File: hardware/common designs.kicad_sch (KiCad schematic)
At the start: 121 parts, among them J401 Conn_01x05_Pin, J402 Main Current Hall Effect Sens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, J403 Conn_02x03_Top_Bottom, K401 G5Q-1A 12Vdc, K402 G5Q-1A 24Vdc, Q401 MMBT5550L, Q402 MMBTA94, Q403 MMBT5550L, Q404 MMBT5550L, Q405 TSM2328CX, Q406 TSM2328CX, Q407 TSM2328CX, Q408 TSM2328CX, U401 IPD70R, U402 NSI45015, U403 MIC7300M5, U404 MCP2542FDxMF, U405 DMN62D0U, U406 IPD14N06, U407 NSI5030, U408 Si1450DH, U409 MCP9700x-ETT, U410 AP7381-33SA-7, U411 ISOM8110DFS, U412 LM74502, U413 TLP176AM, U414 NCV68061, U415 ISO1044BD, U416 TLV713185PDBV, U417 AP64060ZQ, U418 AP64060ZQ, U419 RAA211805, U420 IRS20752, U421 MC7815C, U422 IPD14N06, U423 AP7384-50SA, U501 TC74HC595

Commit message: we love ti
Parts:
- added C501: 1u, Capacitor_SMD:C_0603_1608Metric_Pad1.08x0.95mm_HandSolder, symbol Device:C_Small
- added Q501: DI035P04PT, zzLocalLibraries-Footprints:D_QFN_3.3x3.3mm_P0.65mm, symbol zzLocalLibrary:DI035P04PT
- U411: mouser 1 (none) -> https://www.mouser.com/ProductDetail/Texas-Instruments/ISOM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

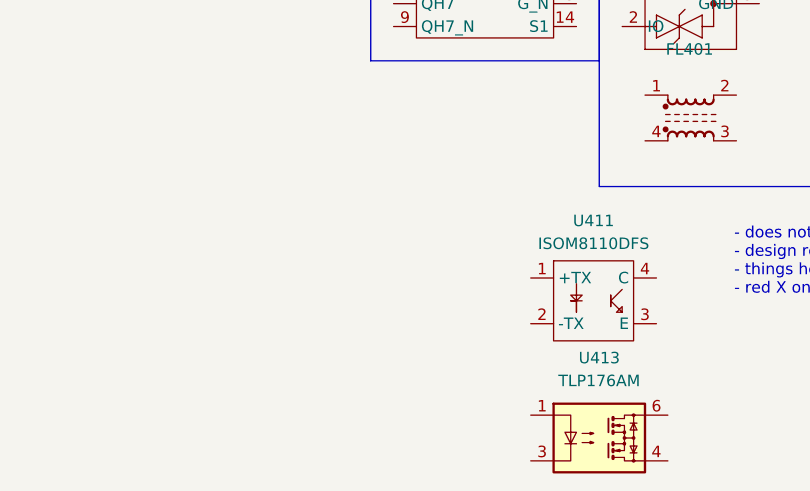
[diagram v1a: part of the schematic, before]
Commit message: new psu
now not under sized
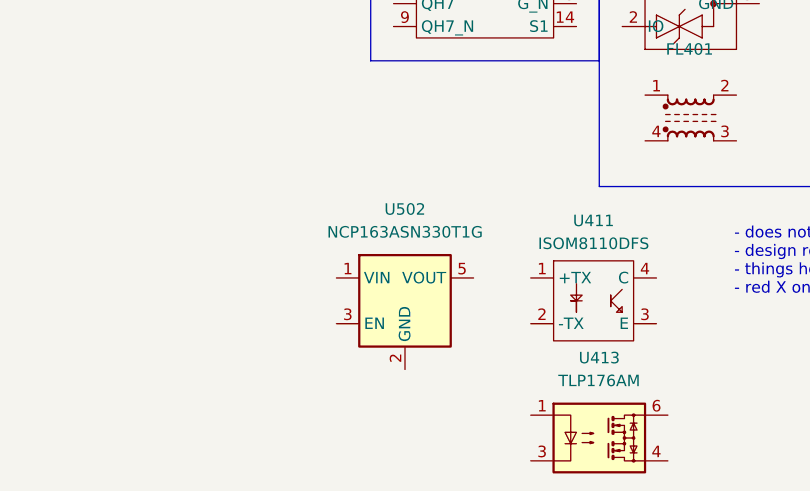
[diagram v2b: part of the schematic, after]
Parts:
- added U502: NCP163ASN330T1G, Package_TO_SOT_SMD:SOT-23-5_HandSoldering, symbol Regulator_Linear:NCP163ASN330T1G

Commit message: lsoing it
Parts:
- removed FL401: Choke_CommonMode_FerriteCore_1243, Inductor_SMD:L_CommonModeChoke_Coilcraft_1812CAN, symbol Filter:Choke_CommonMode_FerriteCore_1243
- added C308: 22u, Capacitor_SMD:C_0805_2012Metric_Pad1.18x1.45mm_HandSolder, symbol Device:C_Small
- added FL801: Choke_CommonMode_FerriteCore_1243, Inductor_SMD:L_CommonModeChoke_Coilcraft_1812CAN, symbol Filter:Choke_CommonMode_FerriteCore_1243
- added R304: 33.2k, Resistor_SMD:R_0805_2012Metric_Pad1.20x1.40mm_HandSolder, symbol Device:R_Small_US
- renumbered C501 to C307, C401 to C801, C402 to C802, C403 to C803, C404 to C804, C405 to C805, C406 to C806, C407 to C807, C408 to C808, C409 to C809, C410 to C810, C411 to C811, C412 to C812, C413 to C813, C414 to C814, C415 to C815, C416 to C816, C417 to C817, C418 to C818, C419 to C819, C420 to C820, C421 to C821, C422 to C822, CR401 to CR801, D401 to D801, D402 to D802, D403 to D803, D404 to D804, D405 to D805, D406 to D806, D407 to D807, D408 to D808, D409 to D809, D410 to D810, D411 to D811, D412 to D812, D413 to D813, D414 to D814, D415 to D815, D416 to D816, FB401 to FB801, FB402 to FB802, J401 to J801, J402 to J802, J403 to J803, K401 to K801, K402 to K802, L401 to L801, L402 to L802, L403 to L803, Q501 to Q303, Q401 to Q801, Q402 to Q802, Q405 to Q803, Q403 to Q804, Q404 to Q805, Q406 to Q806, Q407 to Q807, Q408 to Q808, R401 to R801, R402 to R802, R403 to R803, R404 to R804, R405 to R805, R406 to R806, R407 to R807, R408 to R808, R409 to R809, R410 to R810, R411 to R811, R412 to R812, R413 to R813, R414 to R814, R415 to R815, R416 to R816, R417 to R817, R418 to R818, R419 to R819, R420 to R820, R421 to R821, R422 to R822, R438 to R823, R423 to R824, R424 to R825, R425 to R826, R426 to R827, R427 to R828, R428 to R829, R429 to R830, R430 to R831, R431 to R832, R432 to R833, R433 to R834, R434 to R835, R435 to R836, R436 to R837, R437 to R838, TP401 to TP801, U502 to U302, U501 to U303, U401 to U801, U402 to U802, U403 to U803, U404 to U804, U405 to U805, U406 to U806, U407 to U807, U408 to U808, U409 to U809, U410 to U810, U412 to U811, U414 to U812, U416 to U813, U417 to U814, U418 to U815, U419 to U816, U420 to U817, U421 to U818, U422 to U819, U423 to U820, U415 to U821, U411 to U822, U413 to U823

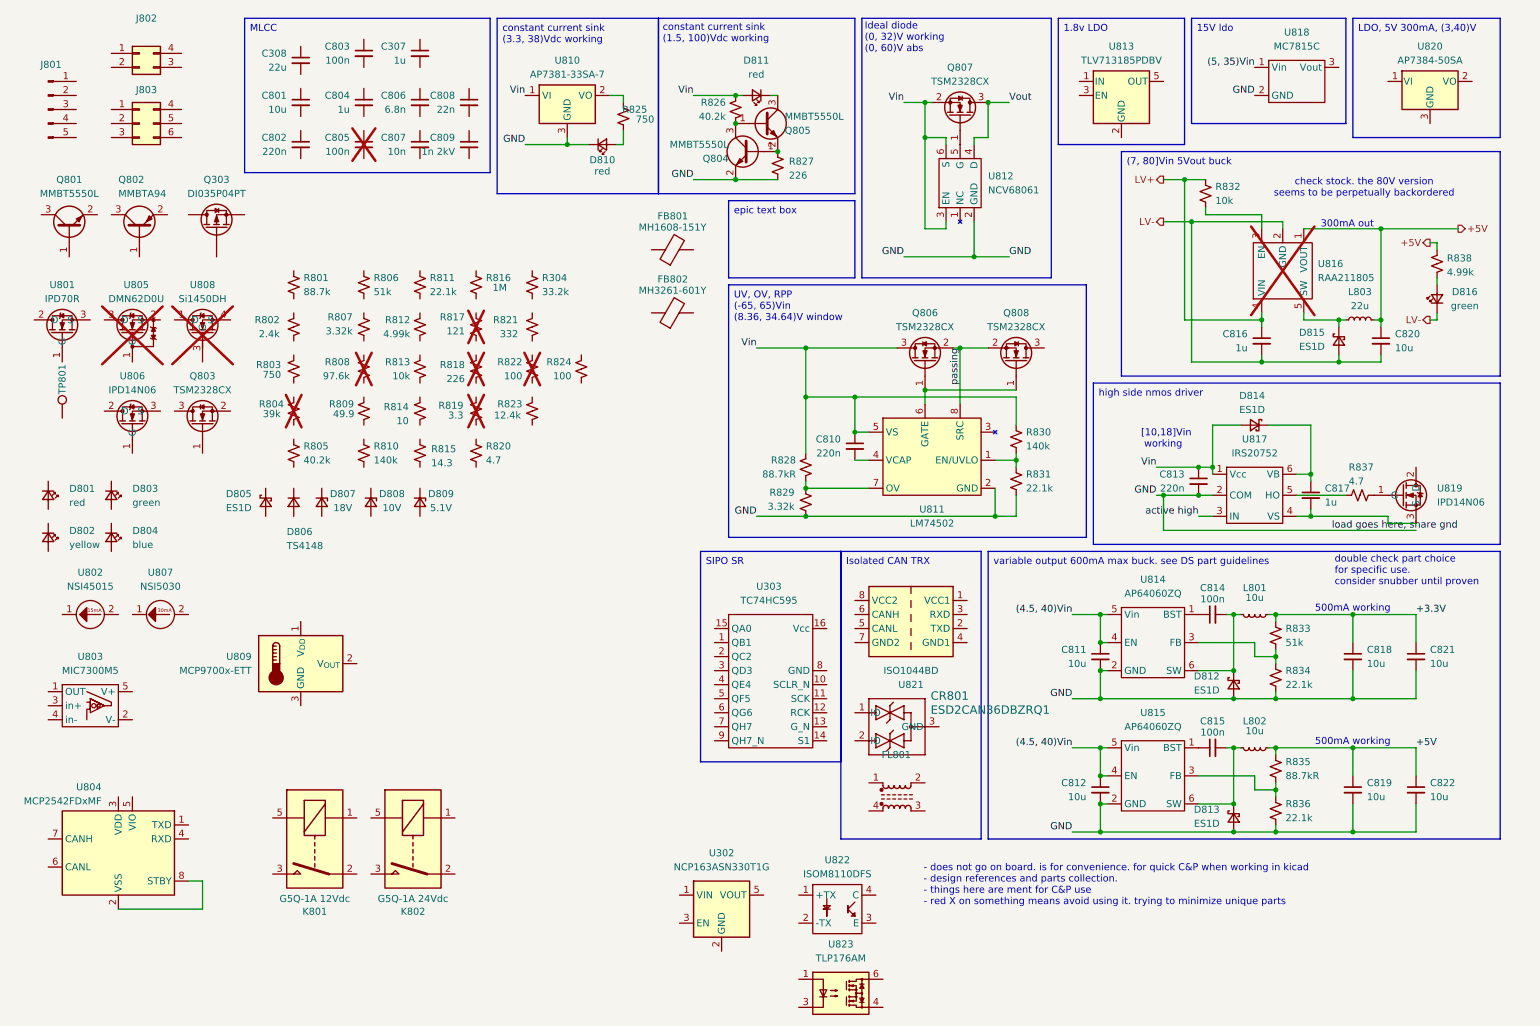
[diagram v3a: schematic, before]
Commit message: updated 3d models
freecad my belovid
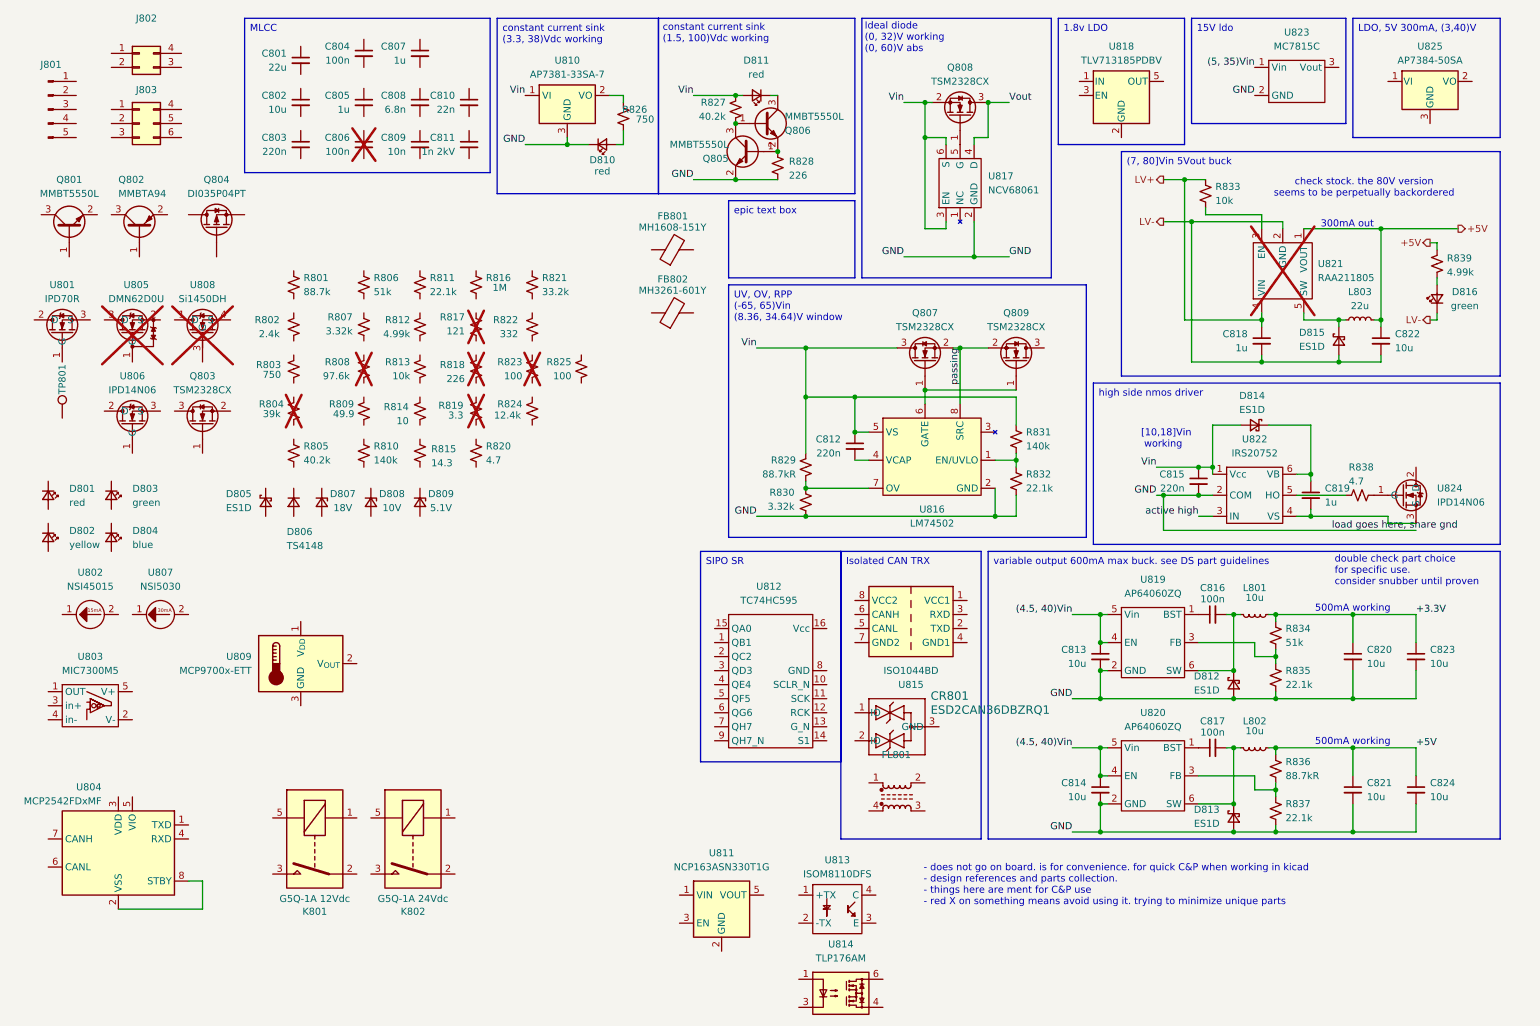
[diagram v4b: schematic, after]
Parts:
- renumbered C308 to C801, C801 to C802, C802 to C803, C803 to C804, C804 to C805, C805 to C806, C307 to C807, C806 to C808, C807 to C809, C808 to C810, C809 to C811, C810 to C812, C811 to C813, C812 to C814, C813 to C815, C814 to C816, C815 to C817, C816 to C818, C817 to C819, C818 to C820, C819 to C821, C820 to C822, C821 to C823, C822 to C824, Q303 to Q804, Q804 to Q805, Q805 to Q806, Q806 to Q807, Q807 to Q808, Q808 to Q809, R304 to R821, R821 to R822, R822 to R823, R823 to R824, R824 to R825, R825 to R826, R826 to R827, R827 to R828, R828 to R829, R829 to R830, R830 to R831, R831 to R832, R832 to R833, R833 to R834, R834 to R835, R835 to R836, R836 to R837, R837 to R838, R838 to R839, U302 to U811, U303 to U812, U822 to U813, U823 to U814, U821 to U815, U811 to U816, U812 to U817, U813 to U818, U814 to U819, U815 to U820, U816 to U821, U817 to U822, U818 to U823, U819 to U824, U820 to U825

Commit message: maby
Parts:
- C999: renamed from C801; specs 22uF, 25V, 20%, X5R, -55C, +85C -> 22uF, 25V, 20%, X5R, -55C, +85C, mlcc
- renumbered C802 to C401, C803 to C402, C804 to C403, C805 to C404, C806 to C405, C808 to C406, C809 to C407, C810 to C408, C811 to C409, C812 to C410, C813 to C411, C814 to C412, C815 to C413, C816 to C414, C817 to C415, C818 to C416, C819 to C417, C820 to C418, C821 to C419, C822 to C420, C823 to C421, C824 to C422, C807 to C501, CR801 to CR401, D801 to D401, D802 to D402, D803 to D403, D804 to D404, D805 to D405, D806 to D406, D807 to D407, D808 to D408, D809 to D409, D810 to D410, D811 to D411, D812 to D412, D813 to D413, D814 to D414, D815 to D415, D816 to D416, FB801 to FB401, FB802 to FB402, FL801 to FL401, J801 to J401, J802 to J402, J803 to J403, K801 to K401, K802 to K402, L801 to L401, L802 to L402, L803 to L403, Q801 to Q401, Q802 to Q402, Q805 to Q403, Q806 to Q404, Q803 to Q405, Q807 to Q406, Q808 to Q407, Q809 to Q408, Q804 to Q501, R801 to R401, R802 to R402, R803 to R403, R804 to R404, R805 to R405, R806 to R406, R807 to R407, R808 to R408, R809 to R409, R810 to R410, R811 to R411, R812 to R412, R813 to R413, R814 to R414, R815 to R415, R816 to R416, R817 to R417, R818 to R418, R819 to R419, R820 to R420, R822 to R421, R823 to R422, R825 to R423, R826 to R424, R827 to R425, R828 to R426, R829 to R427, R830 to R428, R831 to R429, R832 to R430, R833 to R431, R834 to R432, R835 to R433, R836 to R434, R837 to R435, R838 to R436, R839 to R437, R824 to R438, R821 to R501, TP801 to TP401, U801 to U401, U802 to U402, U803 to U403, U804 to U404, U805 to U405, U806 to U406, U807 to U407, U808 to U408, U809 to U409, U810 to U410, U813 to U411, U816 to U412, U814 to U413, U817 to U414, U815 to U415, U818 to U416, U819 to U417, U820 to U418, U821 to U419, U822 to U420, U823 to U421, U824 to U422, U825 to U423, U812 to U501, U811 to U502
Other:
- moved on the sheet: C999

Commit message: freecad is yippie
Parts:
- FL801: renamed from FL401; footprint Inductor_SMD:L_CommonModeChoke_Coilcraft_1812CAN -> zzLocalLibraries-Footprints:L_CommonModeChoke_Coilcraft_1812CAN
- renumbered C999 to C801, C401 to C802, C402 to C803, C403 to C804, C404 to C805, C405 to C806, C501 to C807, C406 to C808, C407 to C809, C408 to C810, C409 to C811, C410 to C812, C411 to C813, C412 to C814, C413 to C815, C414 to C816, C415 to C817, C416 to C818, C417 to C819, C418 to C820, C419 to C821, C420 to C822, C421 to C823, C422 to C824, CR401 to CR801, D401 to D801, D402 to D802, D403 to D803, D404 to D804, D405 to D805, D406 to D806, D407 to D807, D408 to D808, D409 to D809, D410 to D810, D411 to D811, D412 to D812, D413 to D813, D414 to D814, D415 to D815, D416 to D816, FB401 to FB801, FB402 to FB802, J401 to J801, J402 to J802, J403 to J803, K401 to K801, K402 to K802, L401 to L801, L402 to L802, L403 to L803, Q401 to Q801, Q402 to Q802, Q405 to Q803, Q501 to Q804, Q403 to Q805, Q404 to Q806, Q406 to Q807, Q407 to Q808, Q408 to Q809, R401 to R801, R402 to R802, R403 to R803, R404 to R804, R405 to R805, R406 to R806, R407 to R807, R408 to R808, R409 to R809, R410 to R810, R411 to R811, R412 to R812, R413 to R813, R414 to R814, R415 to R815, R416 to R816, R417 to R817, R418 to R818, R419 to R819, R420 to R820, R501 to R821, R421 to R822, R422 to R823, R438 to R824, R423 to R825, R424 to R826, R425 to R827, R426 to R828, R427 to R829, R428 to R830, R429 to R831, R430 to R832, R431 to R833, R432 to R834, R433 to R835, R434 to R836, R435 to R837, R436 to R838, R437 to R839, TP401 to TP801, U401 to U801, U402 to U802, U403 to U803, U404 to U804, U405 to U805, U406 to U806, U407 to U807, U408 to U808, U409 to U809, U410 to U810, U502 to U811, U501 to U812, U411 to U813, U413 to U814, U415 to U815, U412 to U816, U414 to U817, U416 to U818, U417 to U819, U418 to U820, U419 to U821, U420 to U822, U421 to U823, U422 to U824, U423 to U825

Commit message: oops
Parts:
- FL801: footprint zzLocalLibraries-Footprints:L_CommonModeChoke_Coilcraft_1812CAN -> Inductor_SMD:L_CommonModeChoke_Coilcraft_1812CAN

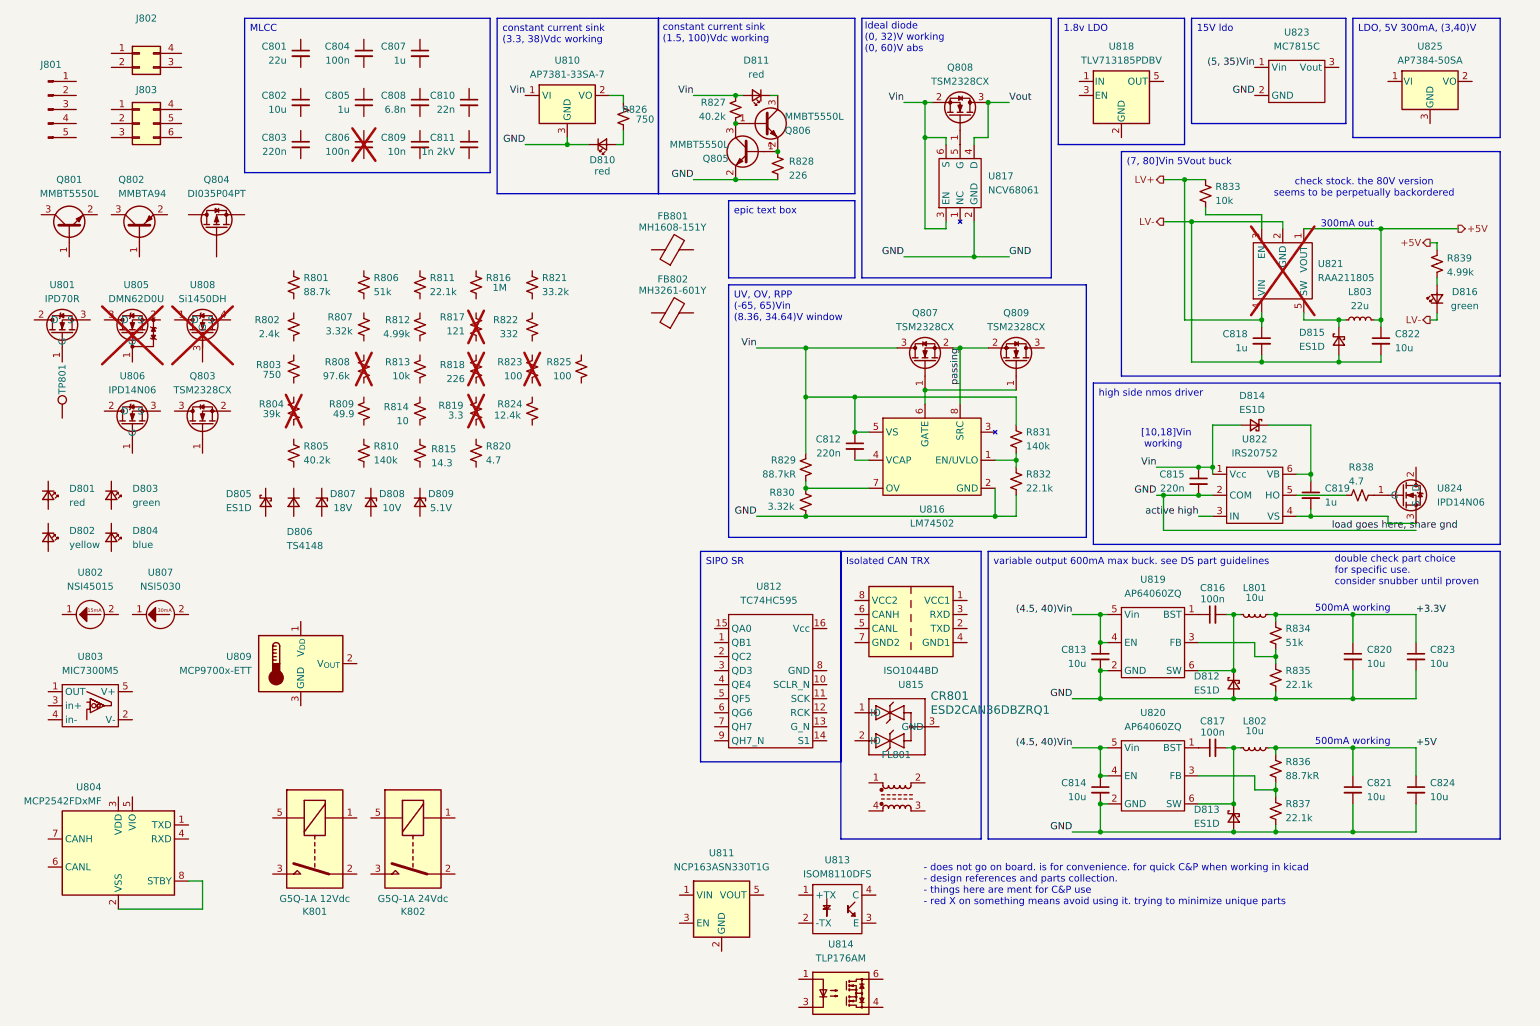
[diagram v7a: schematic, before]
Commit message: rework vt bee
UTA, where CpEs cant make a pcb and CSs cant write any code.
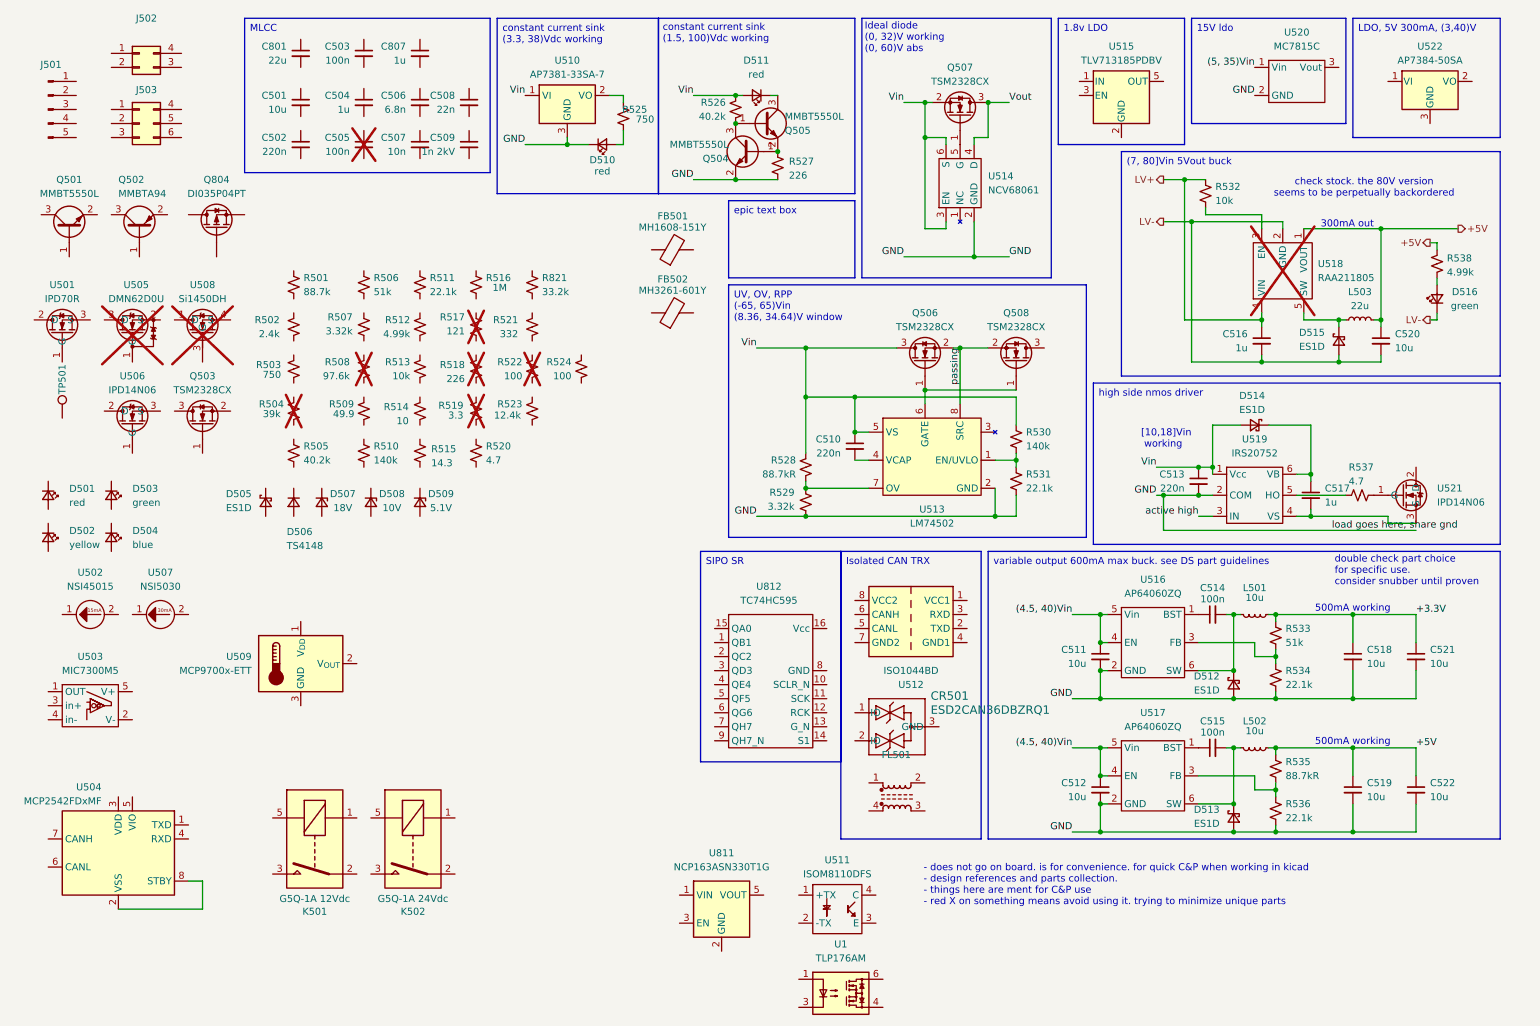
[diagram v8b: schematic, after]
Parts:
- R502: renamed from R802; unit x10 0.039 -> 0.038
- R507: renamed from R807; unit x10 0.019 -> .025
- renumbered C802 to C501, C803 to C502, C804 to C503, C805 to C504, C806 to C505, C808 to C506, C809 to C507, C810 to C508, C811 to C509, C812 to C510, C813 to C511, C814 to C512, C815 to C513, C816 to C514, C817 to C515, C818 to C516, C819 to C517, C820 to C518, C821 to C519, C822 to C520, C823 to C521, C824 to C522, CR801 to CR501, D801 to D501, D802 to D502, D803 to D503, D804 to D504, D805 to D505, D806 to D506, D807 to D507, D808 to D508, D809 to D509, D810 to D510, D811 to D511, D812 to D512, D813 to D513, D814 to D514, D815 to D515, D816 to D516, FB801 to FB501, FB802 to FB502, FL801 to FL501, J801 to J501, J802 to J502, J803 to J503, K801 to K501, K802 to K502, L801 to L501, L802 to L502, L803 to L503, Q801 to Q501, Q802 to Q502, Q803 to Q503, Q805 to Q504, Q806 to Q505, Q807 to Q506, Q808 to Q507, Q809 to Q508, R801 to R501, R803 to R503, R804 to R504, R805 to R505, R806 to R506, R808 to R508, R809 to R509, R810 to R510, R811 to R511, R812 to R512, R813 to R513, R814 to R514, R815 to R515, R816 to R516, R817 to R517, R818 to R518, R819 to R519, R820 to R520, R822 to R521, R823 to R522, R824 to R523, R825 to R524, R826 to R525, R827 to R526, R828 to R527, R829 to R528, R830 to R529, R831 to R530, R832 to R531, R833 to R532, R834 to R533, R835 to R534, R836 to R535, R837 to R536, R838 to R537, R839 to R538, TP801 to TP501, U814 to U1, U801 to U501, U802 to U502, U803 to U503, U804 to U504, U805 to U505, U806 to U506, U807 to U507, U808 to U508, U809 to U509, U810 to U510, U813 to U511, U815 to U512, U816 to U513, U817 to U514, U818 to U515, U819 to U516, U820 to U517, U821 to U518, U822 to U519, U823 to U520, U824 to U521, U825 to U522
